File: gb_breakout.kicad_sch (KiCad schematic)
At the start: 21 parts, among them IC1 74LVC16T245DGGRG4, IC2 74LVC16T245DGGRG4, IC3 SN74LVC1T45DBVT, J1 Conn_02x16_Counter_Clockwise, U1 Cartridge_Bus

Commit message: remove SN74LVC1T45 library & references since it's not what I need
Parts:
- removed IC3: SN74LVC1T45DBVT, SN74LVC1T45DBVT:SOT95P280X145-6N, symbol SN74LVC1T45DBVT:SN74LVC1T45DBVT
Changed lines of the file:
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@@
-    )
-  )
-  (symbol (lib_id "SN74LVC1T45DBVT:SN74LVC1T45DBVT") (at 121.92 167.64 0) (unit 1)
-    (in_bom yes) (on_board yes) (dnp no) (fields_autoplaced)
-    (property "Reference" "IC3" (at 135.89 161.29 0)
-      (effects (font (size 1.27 1.27)))
-    )
-    (property "Value" "SN74LVC1T45DBVT" (at 135.89 163.83 0)
-      (effects (font (size 1.27 1.27)))
-    )
-    (property "Footprint" "SN74LVC1T45DBVT:SOT95P280X145-6N" (at 146.05 262.56 0)
-      (effects (font (size 1.27 1.27)) (justify left top) hide)
-    )
-    (property "Datasheet" "http://www.ti.com/lit/ds/symlink/sn74lvc1t45.pdf" (at 146.05 362.56 0)
-      (effects (font (size 1.27 1.27)) (justify left top) hide)
-    )
-    (property "Height" "1.45" (at 146.05 562.56 0)
-      (effects (font (size 1.27 1.27)) (justify left top) hide)
-    )
-    (property "Mouser Part Number" "595-SN74LVC1T45DBVT" (at 146.05 662.56 0)
-      (effects (font (size 1.27 1.27)) (justify left top) hide)
-    )
-    (property "Mouser Price/Stock" "https://www.mouser.co.uk/ProductDetail/Texas-Instruments/SN74LVC1T45DBVT?qs=pajgIaoyDUiBRX7GYR%252BH8g%3D%3D" (at 146.05 762.56 0)
-      (effects (font (size 1.27 1.27)) (justify left top) hide)
-    )
-    (property "Manufacturer_Name" "Texas Instruments" (at 146.05 862.56 0)
-      (effects (font (size 1.27 1.27)) (justify left top) hide)
-    )
-    (property "Manufacturer_Part_Number" "SN74LVC1T45DBVT" (at 146.05 962.56 0)
-      (effects (font (size 1.27 1.27)) (justify left top) hide)
-    )
-    (pin "1")
-    (pin "2")
-    (pin "3")
-    (pin "4")
-    (pin "5")
-    (pin "6")
-    (instances
-      (project "gb_breakout"
-        (path "/e63e39d7-6ac0-4ffd-8aa3-1841a4541b55"
-          (reference "IC3") (unit 1)
-        )
-      )
     )
   )

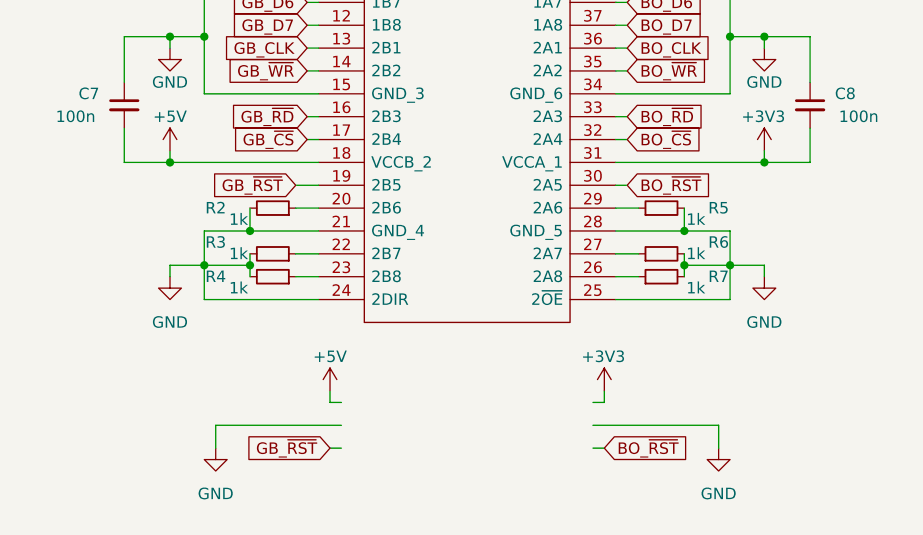
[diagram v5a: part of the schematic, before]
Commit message: add open drain buffer to reset line
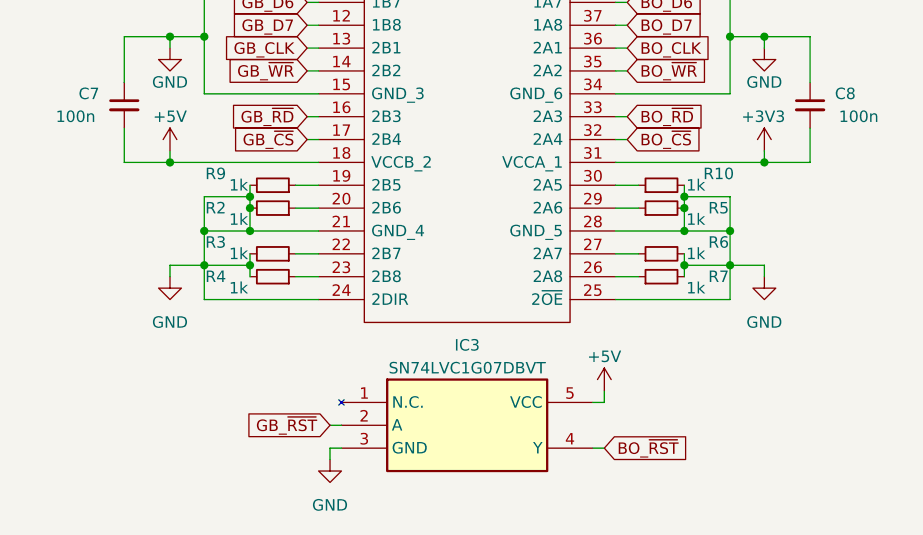
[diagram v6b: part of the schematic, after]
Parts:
- added IC3: SN74LVC1G07DBVT, SOT95P280X145-5N, symbol SN74LVC1G07DBVT:SN74LVC1G07DBVT
- added R10, R9: 1k, Resistor_SMD:R_0402_1005Metric, symbol Device:R_Small
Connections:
- net +5V: now also IC3.5 (VCC)
- net BO_~{RST}: now also IC3.4 (Y); no longer IC2.30 (2A5)
- net GB_~{RST}: now also IC3.2 (A); no longer IC2.19 (2B5)
- net GND: now also IC3.3 (GND), R10.2, R9.2
- new net: IC2.30 (2A5), R10.1
- new net: IC2.19 (2B5), R9.1

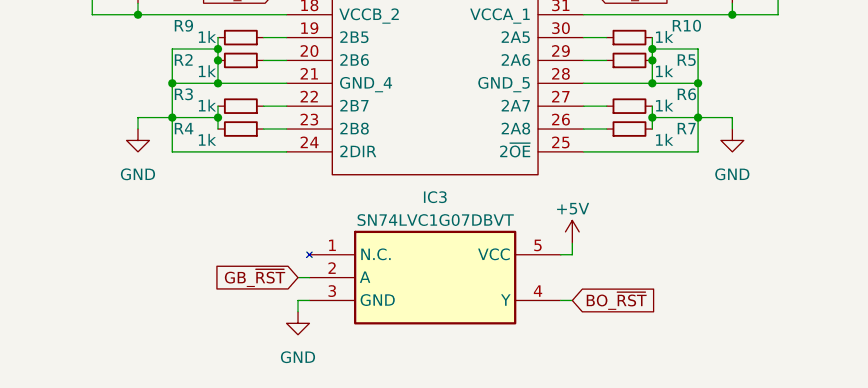
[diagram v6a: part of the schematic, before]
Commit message: route open drain buffer on PCB
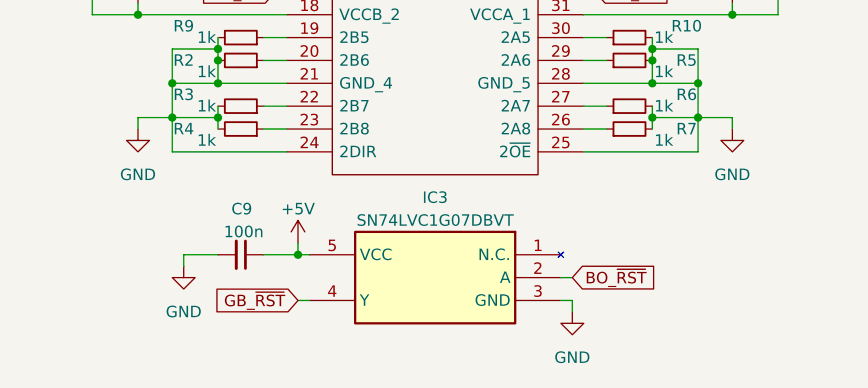
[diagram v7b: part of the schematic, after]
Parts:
- added C9: 100n, Capacitor_SMD:C_0603_1608Metric, symbol Device:C_Small
- IC3: footprint SOT95P280X145-5N -> SN74LVC1G07DBVT:SOT95P280X145-5N
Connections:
- net +5V: now also C9.1
- net BO_~{RST}: now also IC3.2 (A); no longer IC3.4 (Y)
- net GB_~{RST}: now also IC3.4 (Y); no longer IC3.2 (A)
- net GND: now also C9.2
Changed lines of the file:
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@@
   (junction (at 102.87 27.94) (diameter 0) (color 0 0 0 0)
   )
+  (junction (at 120.65 167.64) (diameter 0) (color 0 0 0 0)
+  )
   (junction (at 106.68 53.34) (diameter 0) (color 0 0 0 0)
   )
@@
     (stroke (width 0) (type default))
   )
+  (wire (pts (xy 116.84 167.64) (xy 120.65 167.64))
+    (stroke (width 0) (type default))
+  )
   (wire (pts (xy 165.1 74.93) (xy 165.1 78.74))
     (stroke (width 0) (type default))
@@
     (stroke (width 0) (type default))
   )
-  (wire (pts (xy 120.65 172.72) (xy 120.65 173.99))
+  (wire (pts (xy 151.13 172.72) (xy 151.13 173.99))
     (stroke (width 0) (type default))
   )
@@
     (stroke (width 0) (type default))
   )
-  (wire (pts (xy 149.86 167.64) (xy 151.13 167.64))
+  (wire (pts (xy 121.92 167.64) (xy 120.65 167.64))
     (stroke (width 0) (type default))
   )
@@
     (stroke (width 0) (type default))
   )
+  (wire (pts (xy 107.95 167.64) (xy 107.95 168.91))
+    (stroke (width 0) (type default))
+  )
   (wire (pts (xy 198.12 142.24) (xy 198.12 143.51))
     (stroke (width 0) (type default))
@@
     (stroke (width 0) (type default))
   )
-  (wire (pts (xy 149.86 172.72) (xy 151.13 172.72))
+  (wire (pts (xy 121.92 172.72) (xy 120.65 172.72))
     (stroke (width 0) (type default))
   )
@@
     (stroke (width 0) (type default))
   )
+  (wire (pts (xy 111.76 167.64) (xy 107.95 167.64))
+    (stroke (width 0) (type default))
+  )
   (polyline (pts (xy 229.87 43.18) (xy 229.87 48.26))
     (stroke (width 0) (type default))
@@
     (stroke (width 0) (type default))
   )
-  (wire (pts (xy 151.13 167.64) (xy 151.13 166.37))
+  (wire (pts (xy 120.65 167.64) (xy 120.65 166.37))
     (stroke (width 0) (type default))
   )
@@
     (stroke (width 0) (type default))
   )
-  (wire (pts (xy 121.92 172.72) (xy 120.65 172.72))
+  (wire (pts (xy 149.86 172.72) (xy 151.13 172.72))
     (stroke (width 0) (type default))
   )
@@
     (stroke (width 0) (type default))
   )
-  (wire (pts (xy 120.65 170.18) (xy 121.92 170.18))
+  (wire (pts (xy 151.13 170.18) (xy 149.86 170.18))
     (stroke (width 0) (type default))
   )
@@
     )
   )
-  (global_label "BO_~{RST}" (shape input) (at 151.13 172.72 0) (fields_autoplaced)
-    (effects (font (size 1.27 1.27)) (justify left))
-    (property "Intersheetrefs" "${INTERSHEET_REFS}" (at 160.5583 172.6406 0)
-      (effects (font (size 1.27 1.27)) (justify left) hide)
-    )
-  )
   (global_label "GB_A14" (shape input) (at 118.11 77.47 180) (fields_autoplaced)
     (effects (font (size 1.27 1.27)) (justify right))
@@
     )
   )
-  (global_label "GB_~{RST}" (shape input) (at 120.65 170.18 180) (fields_autoplaced)
-    (effects (font (size 1.27 1.27)) (justify right))
-    (property "Intersheetrefs" "${INTERSHEET_REFS}" (at 111.2821 170.1006 0)
-      (effects (font (size 1.27 1.27)) (justify right) hide)
-    )
-  )
   (global_label "GB_~{WR}" (shape input) (at 118.11 130.81 180) (fields_autoplaced)
     (effects (font (size 1.27 1.27)) (justify right))
@@
     )
   )
+  (global_label "GB_~{RST}" (shape input) (at 120.65 172.72 180) (fields_autoplaced)
+    (effects (font (size 1.27 1.27)) (justify right))
+    (property "Intersheetrefs" "${INTERSHEET_REFS}" (at 110.7895 172.72 0)
+      (effects (font (size 1.27 1.27)) (justify right) hide)
+    )
+  )
   (global_label "GB_A7" (shape input) (at 118.11 52.07 180) (fields_autoplaced)
     (effects (font (size 1.27 1.27)) (justify right))
@@
     )
   )
+  (global_label "BO_~{RST}" (shape input) (at 151.13 170.18 0) (fields_autoplaced)
+    (effects (font (size 1.27 1.27)) (justify left))
+    (property "Intersheetrefs" "${INTERSHEET_REFS}" (at 161.051 170.18 0)
+      (effects (font (size 1.27 1.27)) (justify left) hide)
+    )
+  )
   (global_label "GB_~{WR}" (shape input) (at 118.11 97.79 180) (fields_autoplaced)
     (effects (font (size 1.27 1.27)) (justify right))
@@
     )
   )
-  (symbol (lib_id "SN74LVC1G07DBVT:SN74LVC1G07DBVT") (at 121.92 167.64 0) (unit 1)
+  (symbol (lib_id "SN74LVC1G07DBVT:SN74LVC1G07DBVT") (at 149.86 167.64 0) (mirror y) (unit 1)
     (in_bom yes) (on_board yes) (dnp no) (fields_autoplaced)
     (property "Reference" "IC3" (at 135.89 161.29 0)
@@
       (effects (font (size 1.27 1.27)))
     )
-    (property "Footprint" "SOT95P280X145-5N" (at 146.05 262.56 0)
+    (property "Footprint" "SN74LVC1G07DBVT:SOT95P280X145-5N" (at 125.73 262.56 0)
       (effects (font (size 1.27 1.27)) (justify left top) hide)
     )
-    (property "Datasheet" "http://www.ti.com/lit/gpn/sn74lvc1g07" (at 146.05 362.56 0)
+    (property "Datasheet" "http://www.ti.com/lit/gpn/sn74lvc1g07" (at 125.73 362.56 0)
       (effects (font (size 1.27 1.27)) (justify left top) hide)
     )
-    (property "Height" "1.45" (at 146.05 562.56 0)
+    (property "Height" "1.45" (at 125.73 562.56 0)
       (effects (font (size 1.27 1.27)) (justify left top) hide)
     )
-    (property "Mouser Part Number" "595-SN74LVC1G07DBVT" (at 146.05 662.56 0)
+    (property "Mouser Part Number" "595-SN74LVC1G07DBVT" (at 125.73 662.56 0)
       (effects (font (size 1.27 1.27)) (justify left top) hide)
     )
-    (property "Mouser Price/Stock" "https://www.mouser.co.uk/ProductDetail/Texas-Instruments/SN74LVC1G07DBVT?qs=pajgIaoyDUjU1UIYfW1NgQ%3D%3D" (at 146.05 762.56 0)
+    (property "Mouser Price/Stock" "https://www.mouser.co.uk/ProductDetail/Texas-Instruments/SN74LVC1G07DBVT?qs=pajgIaoyDUjU1UIYfW1NgQ%3D%3D" (at 125.73 762.56 0)
       (effects (font (size 1.27 1.27)) (justify left top) hide)
     )
-    (property "Manufacturer_Name" "Texas Instruments" (at 146.05 862.56 0)
+    (property "Manufacturer_Name" "Texas Instruments" (at 125.73 862.56 0)
       (effects (font (size 1.27 1.27)) (justify left top) hide)
     )
-    (property "Manufacturer_Part_Number" "SN74LVC1G07DBVT" (at 146.05 962.56 0)
+    (property "Manufacturer_Part_Number" "SN74LVC1G07DBVT" (at 125.73 962.56 0)
       (effects (font (size 1.27 1.27)) (justify left top) hide)
     )
@@
     )
   )
+  (symbol (lib_id "Device:C_Small") (at 114.3 167.64 270) (unit 1)
+    (in_bom yes) (on_board yes) (dnp no)
+    (property "Reference" "C9" (at 115.57 162.56 90)
+      (effects (font (size 1.27 1.27)) (justify right))
+    )
+    (property "Value" "100n" (at 116.84 165.1 90)
+      (effects (font (size 1.27 1.27)) (justify right))
+    )
+    (property "Footprint" "Capacitor_SMD:C_0603_1608Metric" (at 114.3 167.64 0)
+      (effects (font (size 1.27 1.27)) hide)
+    )
+    (property "Datasheet" "~" (at 114.3 167.64 0)
+      (effects (font (size 1.27 1.27)) hide)
+    )
+    (pin "1")
+    (pin "2")
+    (instances
+      (project "gb_breakout"
+        (path "/e63e39d7-6ac0-4ffd-8aa3-1841a4541b55"
+          (reference "C9") (unit 1)
+        )
+      )
+    )
+  )
   (symbol (lib_id "Device:R_Small") (at 157.48 143.51 90) (unit 1)
     (in_bom yes) (on_board yes) (dnp no)
@@
     )
   )
-  (symbol (lib_id "power:GND") (at 120.65 173.99 0) (unit 1)
+  (symbol (lib_id "power:GND") (at 151.13 173.99 0) (mirror y) (unit 1)
     (in_bom yes) (on_board yes) (dnp no) (fields_autoplaced)
-    (property "Reference" "#PWR017" (at 120.65 180.34 0)
+    (property "Reference" "#PWR017" (at 151.13 180.34 0)
       (effects (font (size 1.27 1.27)) hide)
     )
-    (property "Value" "GND" (at 120.65 179.07 0)
+    (property "Value" "GND" (at 151.13 179.07 0)
       (effects (font (size 1.27 1.27)))
     )
-    (property "Footprint" "" (at 120.65 173.99 0)
+    (property "Footprint" "" (at 151.13 173.99 0)
       (effects (font (size 1.27 1.27)) hide)
     )
-    (property "Datasheet" "" (at 120.65 173.99 0)
+    (property "Datasheet" "" (at 151.13 173.99 0)
       (effects (font (size 1.27 1.27)) hide)
     )
@@
     )
   )
+  (symbol (lib_id "power:GND") (at 107.95 168.91 0) (mirror y) (unit 1)
+    (in_bom yes) (on_board yes) (dnp no) (fields_autoplaced)
+    (property "Reference" "#PWR015" (at 107.95 175.26 0)
+      (effects (font (size 1.27 1.27)) hide)
+    )
+    (property "Value" "GND" (at 107.95 173.99 0)
+      (effects (font (size 1.27 1.27)))
+    )
+    (property "Footprint" "" (at 107.95 168.91 0)
+      (effects (font (size 1.27 1.27)) hide)
+    )
+    (property "Datasheet" "" (at 107.95 168.91 0)
+      (effects (font (size 1.27 1.27)) hide)
+    )
+    (pin "1")
+    (instances
+      (project "gb_breakout"
+        (path "/e63e39d7-6ac0-4ffd-8aa3-1841a4541b55"
+          (reference "#PWR015") (unit 1)
+        )
+      )
+    )
+  )
   (symbol (lib_id "power:+5V") (at 102.87 39.37 0) (unit 1)
     (in_bom yes) (on_board yes) (dnp no)
@@
     )
   )
-  (symbol (lib_id "power:+5V") (at 151.13 166.37 0) (unit 1)
+  (symbol (lib_id "power:+5V") (at 120.65 166.37 0) (mirror y) (unit 1)
     (in_bom yes) (on_board yes) (dnp no)
-    (property "Reference" "#PWR013" (at 151.13 170.18 0)
+    (property "Reference" "#PWR013" (at 120.65 170.18 0)
       (effects (font (size 1.27 1.27)) hide)
     )
-    (property "Value" "+5V" (at 151.13 162.56 0)
+    (property "Value" "+5V" (at 120.65 162.56 0)
       (effects (font (size 1.27 1.27)))
     )
-    (property "Footprint" "" (at 151.13 166.37 0)
+    (property "Footprint" "" (at 120.65 166.37 0)
       (effects (font (size 1.27 1.27)) hide)
     )
-    (property "Datasheet" "" (at 151.13 166.37 0)
+    (property "Datasheet" "" (at 120.65 166.37 0)
       (effects (font (size 1.27 1.27)) hide)
     )
